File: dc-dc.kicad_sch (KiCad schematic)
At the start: 130 parts, among them SW3 CVS-02B, U30 NCP718ASN500T1G, U31 MPM54304GMN, U32 MPM54304GMN, U33 MAX16150AUT+T, U34 NCP451AFCT2G, U35 SN74LVC1G125DBVR, U36 LM3880, U37 MP8869S, U38 TPS7A20185PDQNR, U39 NCP51400MNTXG, U40 XC6230H001ER-G, U41 REF3012AIDBZT

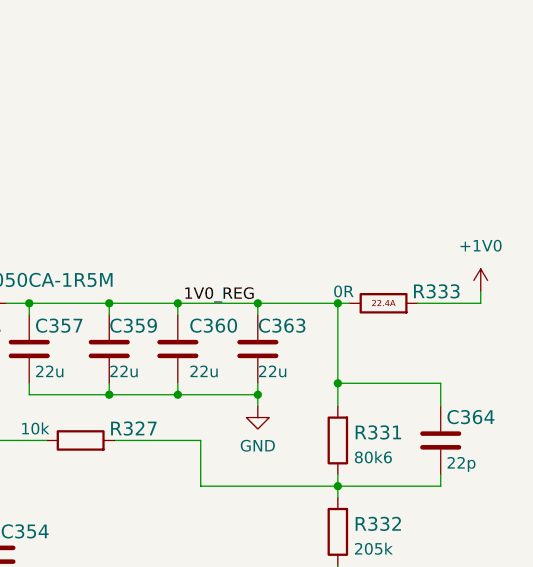
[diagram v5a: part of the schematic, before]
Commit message: Add second 0Ohm for VCORE, placement for PD ideal diode
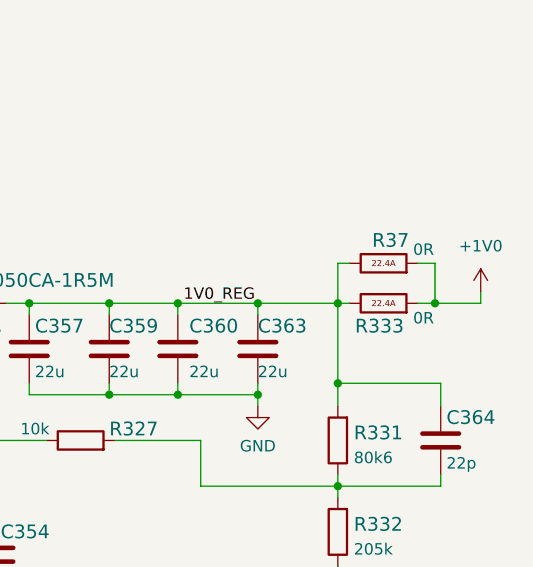
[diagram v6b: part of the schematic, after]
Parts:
- added R37: R_0R_0603_HPWR, antmicro-footprints:0603-res, symbol antmicroResistors0603:R_0R_0603_HPWR
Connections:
- net +1V0: now also R37.2
- net 1V0_REG: now also R37.1
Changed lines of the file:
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@@
   (junction (at 119.38 32.385) (diameter 0) (color 0 0 0 0)
   )
+  (junction (at 398.78 45.085) (diameter 0) (color 0 0 0 0)
+  )
   (junction (at 64.77 229.87) (diameter 0) (color 0 0 0 0)
   )
@@
     (stroke (width 0) (type default) (color 0 0 0 0))
   )
+  (wire (pts (xy 387.985 40.64) (xy 389.255 40.64))
+    (stroke (width 0) (type default) (color 0 0 0 0))
+  )
   (wire (pts (xy 362.585 55.245) (xy 370.205 55.245))
     (stroke (width 0) (type default) (color 0 0 0 0))
@@
     (stroke (width 0) (type default) (color 0 0 0 0))
   )
+  (wire (pts (xy 398.78 40.64) (xy 398.78 45.085))
+    (stroke (width 0) (type default) (color 0 0 0 0))
+  )
   (wire (pts (xy 105.41 118.11) (xy 105.41 104.14))
     (stroke (width 0) (type default) (color 0 0 0 0))
@@
     (stroke (width 0) (type default) (color 0 0 0 0))
   )
-  (wire (pts (xy 403.86 45.085) (xy 396.875 45.085))
+  (wire (pts (xy 403.86 45.085) (xy 398.78 45.085))
     (stroke (width 0) (type default) (color 0 0 0 0))
   )
@@
     (stroke (width 0) (type default) (color 0 0 0 0))
   )
+  (wire (pts (xy 396.875 40.64) (xy 398.78 40.64))
+    (stroke (width 0) (type default) (color 0 0 0 0))
+  )
   (wire (pts (xy 340.995 60.325) (xy 355.6 60.325))
     (stroke (width 0) (type default) (color 0 0 0 0))
@@
     (stroke (width 0) (type default) (color 0 0 0 0))
   )
+  (wire (pts (xy 398.78 45.085) (xy 396.875 45.085))
+    (stroke (width 0) (type default) (color 0 0 0 0))
+  )
   (wire (pts (xy 99.06 133.35) (xy 119.38 133.35))
     (stroke (width 0) (type default) (color 0 0 0 0))
@@
     (stroke (width 0) (type default) (color 0 0 0 0))
   )
+  (wire (pts (xy 387.985 45.085) (xy 387.985 40.64))
+    (stroke (width 0) (type default) (color 0 0 0 0))
+  )
   (wire (pts (xy 184.15 199.39) (xy 189.23 199.39))
     (stroke (width 0) (type default) (color 0 0 0 0))
@@
     (pin "2")
   )
+  (symbol (lib_id "antmicroResistors0603:R_0R_0603_HPWR") (at 393.065 40.64 0) (unit 1)
+    (in_bom yes) (on_board yes)
+    (property "Reference" "R37" (id 0) (at 391.795 38.1 0)
+      (effects (font (size 1.524 1.524)) (justify left))
+    )
+    (property "Value" "R_0R_0603_HPWR" (id 1) (at 393.065 44.45 0)
+      (effects (font (size 1.524 1.524)) hide)
+    )
+    (property "Footprint" "antmicro-footprints:0603-res" (id 2) (at 398.145 35.56 0)
+      (effects (font (size 1.524 1.524)) (justify left) hide)
+    )
+    (property "Datasheet" "" (id 3) (at 393.065 40.64 0)
+      (effects (font (size 1.27 1.27)) hide)
+    )
+    (property "Manufacturer" "ROHM Semiconductor" (id 4) (at 398.145 30.48 0)
+      (effects (font (size 1.524 1.524)) (justify left) hide)
+    )
+    (property "MPN" "PMR03EZPJ000" (id 5) (at 398.145 33.02 0)
+      (effects (font (size 1.524 1.524)) (justify left) hide)
+    )
+    (property "Val" "0R" (id 6) (at 397.51 39.116 0))
+    (pin "1")
+    (pin "2")
+  )
   (symbol (lib_id "power:GND") (at 80.01 243.205 0) (unit 1)
     (in_bom yes) (on_board yes) (fields_autoplaced)
@@
   (symbol (lib_id "antmicroResistors0603:R_0R_0603_HPWR") (at 393.065 45.085 0) (unit 1)
     (in_bom yes) (on_board yes)
-    (property "Reference" "R333" (id 0) (at 396.24 43.815 0)
+    (property "Reference" "R333" (id 0) (at 389.89 47.625 0)
       (effects (font (size 1.524 1.524)) (justify left))
     )
@@
       (effects (font (size 1.524 1.524)) (justify left) hide)
     )
-    (property "Val" "0R" (id 6) (at 388.62 43.815 0))
+    (property "Val" "0R" (id 6) (at 397.51 46.736 0))
     (pin "1")
     (pin "2")

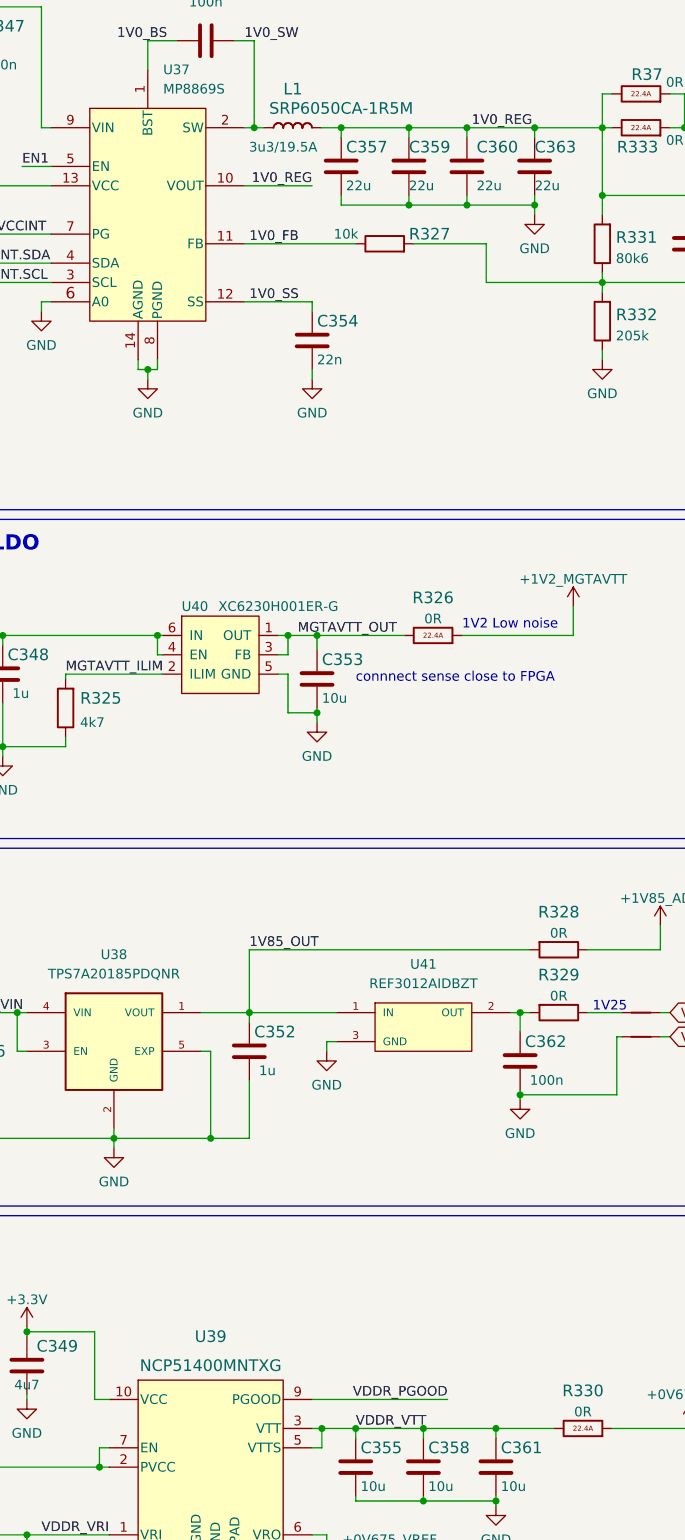
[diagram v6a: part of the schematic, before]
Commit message: Implemented fixes after schematic review
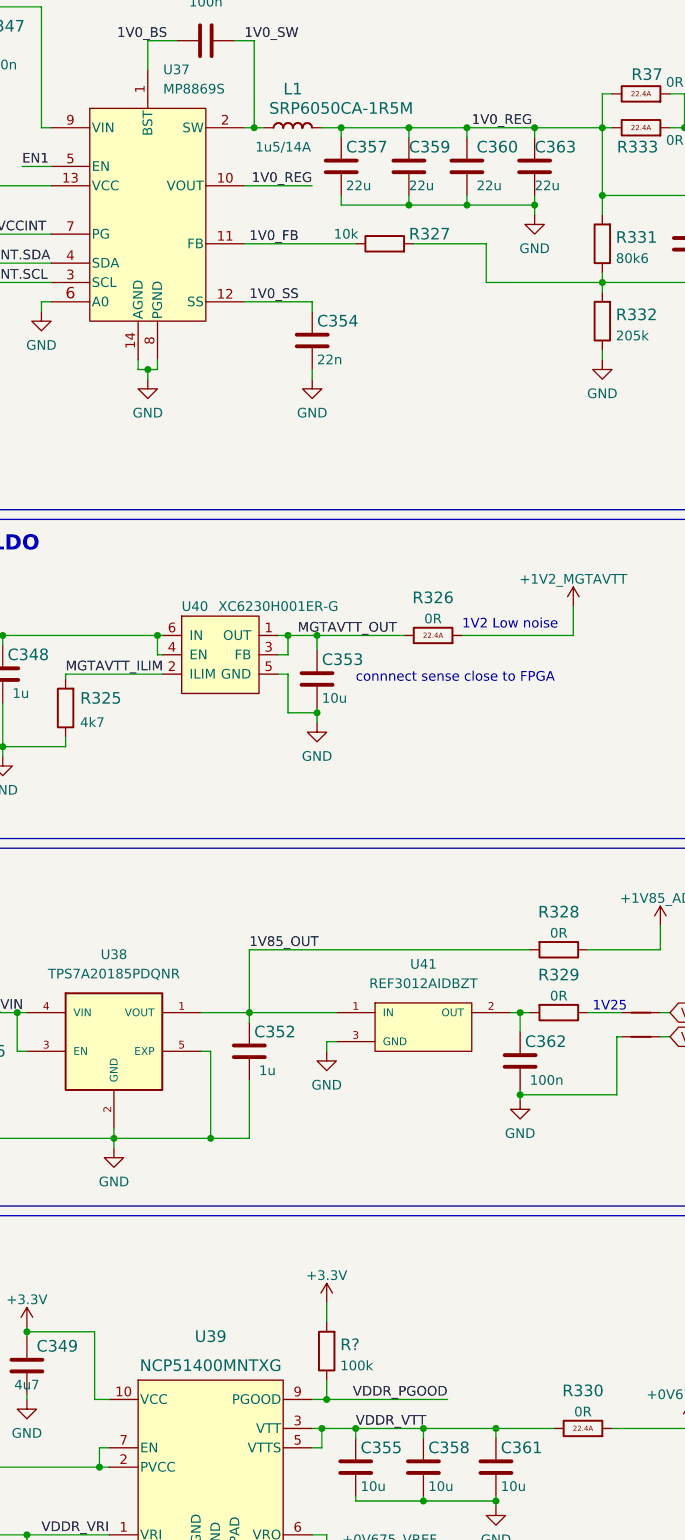
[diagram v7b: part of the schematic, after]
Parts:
- added R?: R_100k_0402, antmicro-footprints:0402-res, symbol antmicroResistors0402:R_100k_0402
- L1: MaxCur 17A -> 14A; Val 3u3/19.5A -> 1u5/14A
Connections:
- net +3V3: now also R?.2
- net VDDR_PGOOD: now also R?.1
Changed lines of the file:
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@@
   (junction (at 150.495 247.015) (diameter 0) (color 0 0 0 0)
   )
+  (junction (at 351.79 212.09) (diameter 0) (color 0 0 0 0)
+  )
   (junction (at 350.52 111.76) (diameter 0) (color 0 0 0 0)
   )
@@
     (stroke (width 0) (type default) (color 0 0 0 0))
   )
+  (wire (pts (xy 351.79 199.39) (xy 351.79 201.93))
+    (stroke (width 0) (type default) (color 0 0 0 0))
+  )
   (wire (pts (xy 119.38 142.24) (xy 119.38 143.51))
     (stroke (width 0) (type default) (color 0 0 0 0))
@@
     (stroke (width 0) (type default) (color 0 0 0 0))
   )
+  (wire (pts (xy 351.79 209.55) (xy 351.79 212.09))
+    (stroke (width 0) (type default) (color 0 0 0 0))
+  )
   (polyline (pts (xy 229.87 136.525) (xy 257.175 136.525))
     (stroke (width 0) (type default) (color 0 0 0 0))
@@
     (stroke (width 0) (type default) (color 0 0 0 0))
   )
-  (wire (pts (xy 349.885 212.09) (xy 367.665 212.09))
+  (wire (pts (xy 349.885 212.09) (xy 351.79 212.09))
     (stroke (width 0) (type default) (color 0 0 0 0))
   )
@@
     (stroke (width 0) (type default) (color 0 0 0 0))
   )
+  (wire (pts (xy 351.79 212.09) (xy 367.665 212.09))
+    (stroke (width 0) (type default) (color 0 0 0 0))
+  )
   (wire (pts (xy 133.35 114.3) (xy 133.35 115.57))
     (stroke (width 0) (type default) (color 0 0 0 0))
@@
       (effects (font (size 1.27 1.27)) (justify left bottom) hide)
     )
-    (property "Datasheet" "" (id 3) (at 374.65 151.13 0)
+    (property "Datasheet" "https://www.ti.com/lit/gpn/REF3012" (id 3) (at 374.65 151.13 0)
       (effects (font (size 1.27 1.27)) (justify left bottom) hide)
     )
@@
     (pin "2")
   )
+  (symbol (lib_id "antmicroResistors0402:R_100k_0402") (at 351.79 205.74 90) (unit 1)
+    (in_bom yes) (on_board yes) (fields_autoplaced)
+    (property "Reference" "R?" (id 0) (at 353.568 204.9054 90)
+      (effects (font (size 1.524 1.524)) (justify right))
+    )
+    (property "Value" "R_100k_0402" (id 1) (at 355.6 205.74 0)
+      (effects (font (size 1.27 1.27)) hide)
+    )
+    (property "Footprint" "antmicro-footprints:0402-res" (id 2) (at 346.71 200.66 0)
+      (effects (font (size 1.524 1.524)) (justify left) hide)
+    )
+    (property "Datasheet" "" (id 3) (at 351.79 205.74 0)
+      (effects (font (size 1.27 1.27)) hide)
+    )
+    (property "Manufacturer" "VISHAY" (id 4) (at 341.63 200.66 0)
+      (effects (font (size 1.524 1.524)) (justify left) hide)
+    )
+    (property "MPN" "CRCW0402100KFKEDHP" (id 5) (at 344.17 200.66 0)
+      (effects (font (size 1.524 1.524)) (justify left) hide)
+    )
+    (property "Val" "100k" (id 6) (at 353.568 207.6705 90)
+      (effects (font (size 1.27 1.27)) (justify right))
+    )
+    (pin "1")
+    (pin "2")
+  )
   (symbol (lib_id "power:+5V") (at 255.905 189.865 0) (unit 1)
     (in_bom yes) (on_board yes) (fields_autoplaced)
@@
     (pin "1")
   )
+  (symbol (lib_id "power:+3.3V") (at 351.79 199.39 0) (unit 1)
+    (in_bom yes) (on_board yes) (fields_autoplaced)
+    (property "Reference" "#PWR?" (id 0) (at 351.79 203.2 0)
+      (effects (font (size 1.27 1.27)) hide)
+    )
+    (property "Value" "+3.3V" (id 1) (at 351.79 195.8142 0))
+    (property "Footprint" "" (id 2) (at 351.79 199.39 0)
+      (effects (font (size 1.27 1.27)) hide)
+    )
+    (property "Datasheet" "" (id 3) (at 351.79 199.39 0)
+      (effects (font (size 1.27 1.27)) hide)
+    )
+    (pin "1")
+  )
   (symbol (lib_id "antmicroResistors0402:R_47k_0402") (at 254.635 41.91 90) (unit 1)
     (in_bom yes) (on_board yes) (fields_autoplaced)
@@
       (effects (font (size 1.27 1.27)) hide)
     )
-    (property "MaxCur" "17A" (id 6) (at 349.25 33.02 0)
+    (property "MaxCur" "14A" (id 6) (at 349.25 33.02 0)
       (effects (font (size 1.27 1.27)) hide)
     )
@@
       (effects (font (size 1.27 1.27)) hide)
     )
-    (property "Val" "3u3/19.5A" (id 8) (at 346.075 47.625 0))
+    (property "Val" "1u5/14A" (id 8) (at 346.075 47.625 0))
     (pin "1")
     (pin "2")

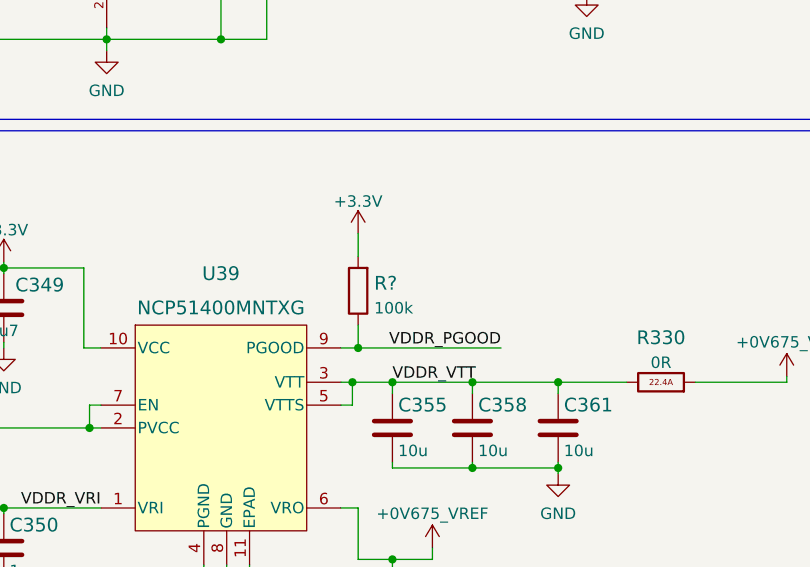
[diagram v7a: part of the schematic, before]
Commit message: Import changes to PCB. Align part of the designators
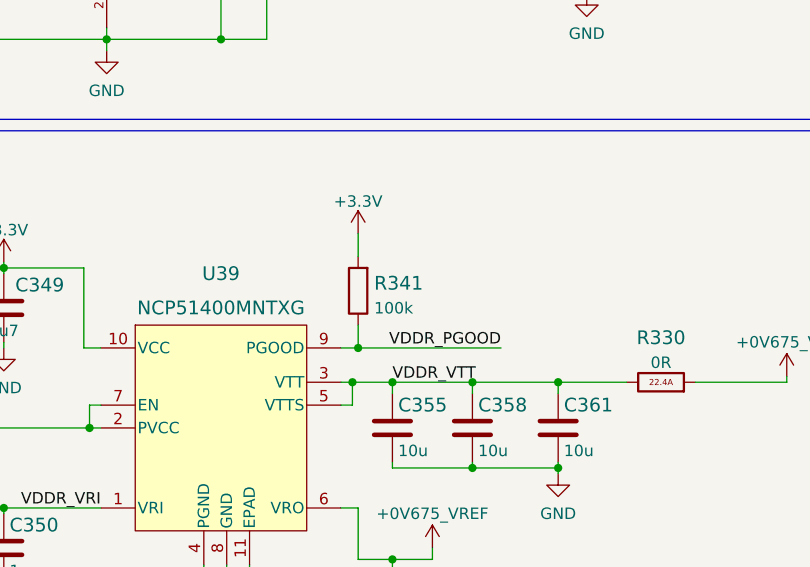
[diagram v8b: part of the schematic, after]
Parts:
- gave numbers to parts that had none: 1
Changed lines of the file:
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@@
   (symbol (lib_id "antmicroResistors0402:R_100k_0402") (at 351.79 205.74 90) (unit 1)
     (in_bom yes) (on_board yes) (fields_autoplaced)
-    (property "Reference" "R?" (id 0) (at 353.568 204.9054 90)
+    (property "Reference" "R341" (id 0) (at 353.568 204.9054 90)
       (effects (font (size 1.524 1.524)) (justify right))
     )
@@
   (symbol (lib_id "power:+3.3V") (at 351.79 199.39 0) (unit 1)
     (in_bom yes) (on_board yes) (fields_autoplaced)
-    (property "Reference" "#PWR?" (id 0) (at 351.79 203.2 0)
+    (property "Reference" "#PWR0460" (id 0) (at 351.79 203.2 0)
       (effects (font (size 1.27 1.27)) hide)
     )
